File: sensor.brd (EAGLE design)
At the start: 15.8 x 15.8 mm, 16 parts

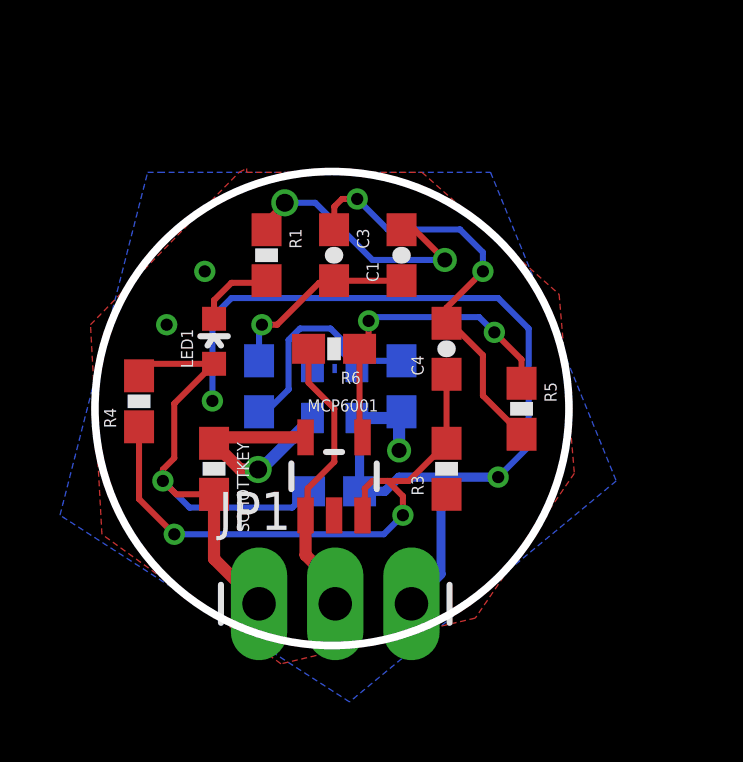
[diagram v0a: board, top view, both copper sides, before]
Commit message: sensor: fix apds-9008 package error
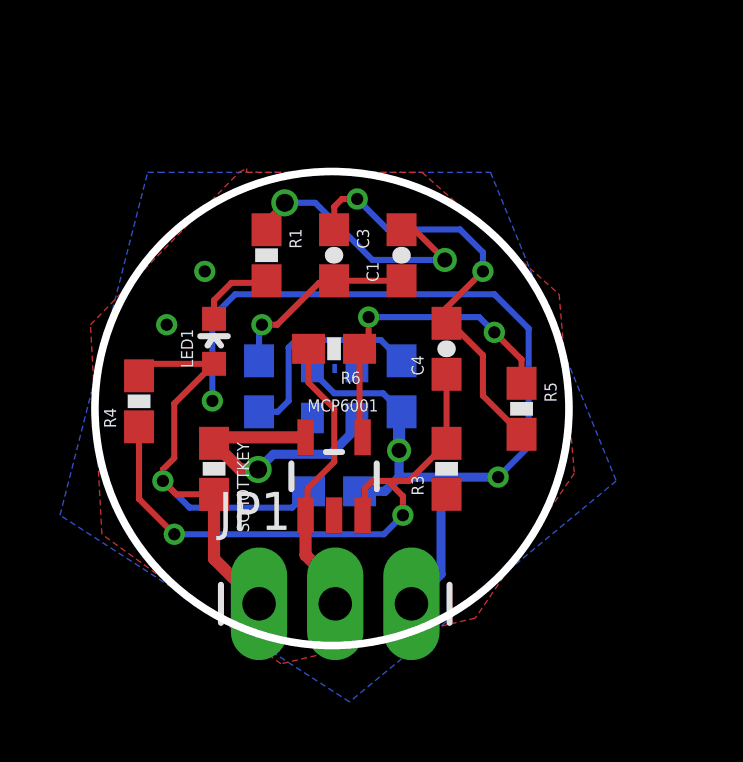
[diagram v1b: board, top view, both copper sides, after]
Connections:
- net GND: now also APDS1.P$4; no longer APDS1.P$3
- net N$7: now also APDS1.P$6; no longer APDS1.P$4
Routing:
- net VDD: track 7.48 -> 9.16 mm
- net GND: track 43.3 -> 44.1 mm
- net N$7: track 7.72 -> 8.52 mm
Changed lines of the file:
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@@
 <wire x1="4.5" y1="7.35" x2="4.7001" y2="7.5501" width="0.4064" layer="1"/>
 <wire x1="4.7001" y1="7.5501" x2="7.55" y2="7.5501" width="0.4064" layer="1"/>
-<wire x1="7.779340625" y1="8.193378125" x2="6.0629625" y2="6.477" width="0.4064" layer="16"/>
-<wire x1="6.0629625" y1="6.477" x2="5.969" y2="6.477" width="0.254" layer="16"/>
 <via x="5.969" y="6.477" extent="1-16" drill="0.6"/>
 <wire x1="5.969" y1="6.477" x2="5.373" y2="6.477" width="0.4064" layer="1"/>
 <wire x1="5.373" y1="6.477" x2="4.5" y2="7.35" width="0.4064" layer="1"/>
+<wire x1="9.260340625" y1="8.193378125" x2="9.260340625" y2="7.863340625" width="0.3048" layer="16"/>
+<wire x1="9.260340625" y1="7.863340625" x2="8.382" y2="6.985" width="0.3048" layer="16"/>
+<wire x1="8.382" y1="6.985" x2="6.477" y2="6.985" width="0.3048" layer="16"/>
+<wire x1="6.477" y1="6.985" x2="5.969" y2="6.477" width="0.3048" layer="16"/>
 </signal>
 <signal name="OUT">
@@
 <contactref element="C2" pad="2"/>
 <contactref element="R2" pad="2"/>
-<contactref element="APDS1" pad="P$4"/>
-<wire x1="6" y1="8.4" x2="6.241" y2="8.4" width="0.2032" layer="16"/>
-<wire x1="6.241" y1="8.4" x2="6.985" y2="9.144" width="0.2032" layer="16"/>
-<wire x1="6.985" y1="9.144" x2="6.985" y2="10.795" width="0.2032" layer="16"/>
-<wire x1="6.985" y1="10.795" x2="7.366" y2="11.176" width="0.2032" layer="16"/>
-<wire x1="7.366" y1="11.176" x2="8.382" y2="11.176" width="0.2032" layer="16"/>
-<wire x1="8.382" y1="11.176" x2="8.763" y2="10.795" width="0.2032" layer="16"/>
-<wire x1="8.763" y1="10.795" x2="8.763" y2="10.39071875" width="0.2032" layer="16"/>
-<wire x1="8.763" y1="10.39071875" x2="9.260340625" y2="9.893378125" width="0.2032" layer="16"/>
-<wire x1="10.75" y1="10.1" x2="9.4669625" y2="10.1" width="0.2032" layer="16"/>
-<wire x1="9.4669625" y1="10.1" x2="9.260340625" y2="9.893378125" width="0.2032" layer="16"/>
+<contactref element="APDS1" pad="P$6"/>
+<wire x1="10.728" y1="10.1" x2="10.75" y2="10.1" width="0.2032" layer="16"/>
+<wire x1="6" y1="8.4" x2="6.622" y2="8.4" width="0.2032" layer="16"/>
+<wire x1="6.622" y1="8.4" x2="6.985" y2="8.763" width="0.2032" layer="16"/>
+<wire x1="6.985" y1="8.763" x2="6.985" y2="10.541" width="0.2032" layer="16"/>
+<wire x1="6.985" y1="10.541" x2="7.239" y2="10.795" width="0.2032" layer="16"/>
+<wire x1="7.239" y1="10.795" x2="9.144" y2="10.795" width="0.2032" layer="16"/>
+<wire x1="9.144" y1="10.795" x2="9.652" y2="10.795" width="0.2032" layer="16"/>
+<wire x1="10.055" y1="10.795" x2="10.75" y2="10.1" width="0.2032" layer="16"/>
+<wire x1="10.055" y1="10.795" x2="9.652" y2="10.795" width="0.2032" layer="16"/>
+<wire x1="9.652" y1="10.795" x2="9.398" y2="10.541" width="0.2032" layer="16"/>
+<wire x1="9.144" y1="10.795" x2="9.398" y2="10.541" width="0.2032" layer="16"/>
+<wire x1="9.398" y1="10.541" x2="9.398" y2="10.0310375" width="0.2032" layer="16"/>
+<wire x1="9.398" y1="10.0310375" x2="9.260340625" y2="9.893378125" width="0.2032" layer="16"/>
 </signal>
 <signal name="N$8">
@@
 <contactref element="MCP6001" pad="4"/>
 <via x="13.843" y="11.049" extent="1-16" drill="0.4064"/>
-<wire x1="9.779" y1="11.557" x2="9.652" y2="11.43" width="0.2032" layer="16"/>
-<via x="9.652" y="11.43" extent="1-16" drill="0.4064"/>
-<wire x1="9.652" y1="11.43" x2="9.652" y2="10.802" width="0.2032" layer="1"/>
+<via x="9.652" y="11.557" extent="1-16" drill="0.4064"/>
+<wire x1="9.652" y1="11.557" x2="9.652" y2="10.802" width="0.2032" layer="1"/>
 <wire x1="9.652" y1="10.802" x2="9.35" y2="10.5" width="0.2032" layer="1"/>
 <wire x1="9.35" y1="10.5" x2="9.35" y2="7.6501" width="0.2032" layer="1"/>
 <wire x1="9.35" y1="7.6501" x2="9.45" y2="7.5501" width="0.2032" layer="1"/>
-<wire x1="9.779" y1="11.557" x2="13.335" y2="11.557" width="0.2032" layer="16"/>
+<wire x1="9.652" y1="11.557" x2="13.335" y2="11.557" width="0.2032" layer="16"/>
 <wire x1="13.335" y1="11.557" x2="13.843" y2="11.049" width="0.2032" layer="16"/>
 <wire x1="13.843" y1="11.049" x2="14.75" y2="10.142" width="0.2032" layer="1"/>
@@
 <contactref element="R3" pad="1"/>
 <contactref element="MCP6001" pad="2"/>
-<contactref element="APDS1" pad="P$3"/>
 <polygon width="0.2032" layer="1" spacing="0.3048" isolate="0.254">
 <vertex x="5.588" y="16.383"/>
@@
 </polygon>
 <via x="4.445" y="8.763" extent="1-16" drill="0.4064"/>
-<wire x1="9.260340625" y1="8.193378125" x2="10.668" y2="8.193378125" width="0.4064" layer="16"/>
 <wire x1="10.75" y1="8.193378125" x2="10.75" y2="8.4" width="0.4064" layer="16"/>
 <wire x1="10.75" y1="8.193378125" x2="10.668" y2="8.193378125" width="0.4064" layer="16"/>
 <wire x1="10.668" y1="8.193378125" x2="10.668" y2="7.112" width="0.4064" layer="16"/>
 <via x="13.97" y="6.223" extent="1-16" drill="0.4064"/>
-<wire x1="9.260340625" y1="8.193378125" x2="9.35" y2="8.193378125" width="0.3048" layer="16"/>
-<wire x1="9.35" y1="8.193378125" x2="9.35" y2="5.75" width="0.3048" layer="16"/>
 <wire x1="9.35" y1="5.75" x2="10.195" y2="5.75" width="0.3048" layer="16"/>
 <wire x1="10.195" y1="5.75" x2="10.668" y2="6.223" width="0.3048" layer="16"/>
@@
 <wire x1="11.185" y1="14.469" x2="10.75" y2="14.469" width="0.2032" layer="1"/>
 <wire x1="4.445" y1="8.763" x2="4.445" y2="11.557" width="0.2032" layer="16"/>
-<wire x1="4.445" y1="11.557" x2="5.08" y2="12.192" width="0.2032" layer="16"/>
-<wire x1="5.08" y1="12.192" x2="13.97" y2="12.192" width="0.2032" layer="16"/>
-<wire x1="13.97" y1="12.192" x2="14.986" y2="11.176" width="0.2032" layer="16"/>
+<wire x1="4.445" y1="11.557" x2="5.207" y2="12.319" width="0.2032" layer="16"/>
+<wire x1="5.207" y1="12.319" x2="13.843" y2="12.319" width="0.2032" layer="16"/>
+<wire x1="13.843" y1="12.319" x2="14.986" y2="11.176" width="0.2032" layer="16"/>
 <wire x1="14.986" y1="11.176" x2="14.986" y2="7.239" width="0.2032" layer="16"/>
 <wire x1="14.986" y1="7.239" x2="13.97" y2="6.223" width="0.2032" layer="16"/>
+<contactref element="APDS1" pad="P$4"/>
+<wire x1="10.668" y1="7.112" x2="10.668" y2="6.223" width="0.3048" layer="16"/>
+<wire x1="10.75" y1="8.493378125" x2="10.75" y2="8.4" width="0.254" layer="16"/>
+<wire x1="7.779340625" y1="9.893378125" x2="7.779340625" y2="9.746659375" width="0.2032" layer="16"/>
+<wire x1="7.779340625" y1="9.746659375" x2="8.509" y2="9.017" width="0.2032" layer="16"/>
+<wire x1="8.509" y1="9.017" x2="10.133" y2="9.017" width="0.2032" layer="16"/>
+<wire x1="10.133" y1="9.017" x2="10.75" y2="8.4" width="0.2032" layer="16"/>
 </signal>
 </signals>

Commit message: sensor: update brd into a 20*20 rectangle
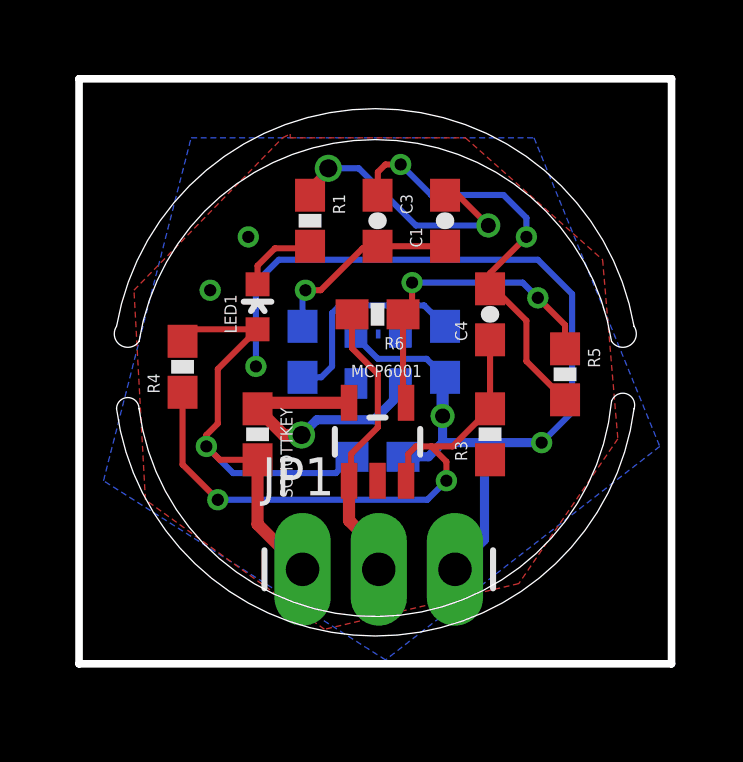
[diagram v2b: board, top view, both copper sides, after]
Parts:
- moved C2 1.85 mm to (7.45, 10.4)
- moved LED1 1.85 mm to (5.95, 11.9)
- moved R1 1.85 mm to (7.70, 14.8)
- moved R4 1.85 mm to (3.45, 9.90)
- moved SCHOTTKEY 1.85 mm to (5.95, 7.65)
- moved JP1 1.85 mm to (7.45, 3.15)
- moved APDS1 1.85 mm to (9.95, 10.2)
- moved C1 1.85 mm to (12.2, 14.8)
- moved C3 1.85 mm to (9.95, 14.8)
- moved C4 1.85 mm to (13.7, 11.7)
- moved C5 1.85 mm to (9.95, 6.90)
- moved MCP6001 1.85 mm to (9.95, 7.40)
- moved R2 1.85 mm to (12.2, 10.4)
- moved R3 1.85 mm to (13.7, 7.65)
- moved R5 1.85 mm to (16.2, 9.65)
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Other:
- board size 15.8 x 15.8 mm -> 19.8 x 19.5 mm
- board text added: "APDS1"
- board text added: "C1"
- board text added: "C2"
- board text added: "C3"
- board text added: "C4"
- board text added: "C5"
- board text added: "JP1"
- board text added: "LED1"
- board text added: "MCP6001"
- board text added: "R1"
- board text added: "R2"
- board text added: "R3"
- board text added: "R4"
- board text added: "R5"
- board text added: "R6"
- board text added: "SCHOTTKEY"

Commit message: sensor: correct schematic and refine layout
1. Replace fake schottkey with a *real* one.
2. Refine polygon.
3. Refine dimension.
4. Refine panel.
5. Add more blowholes (vias).
6. Slightly refine some wires.
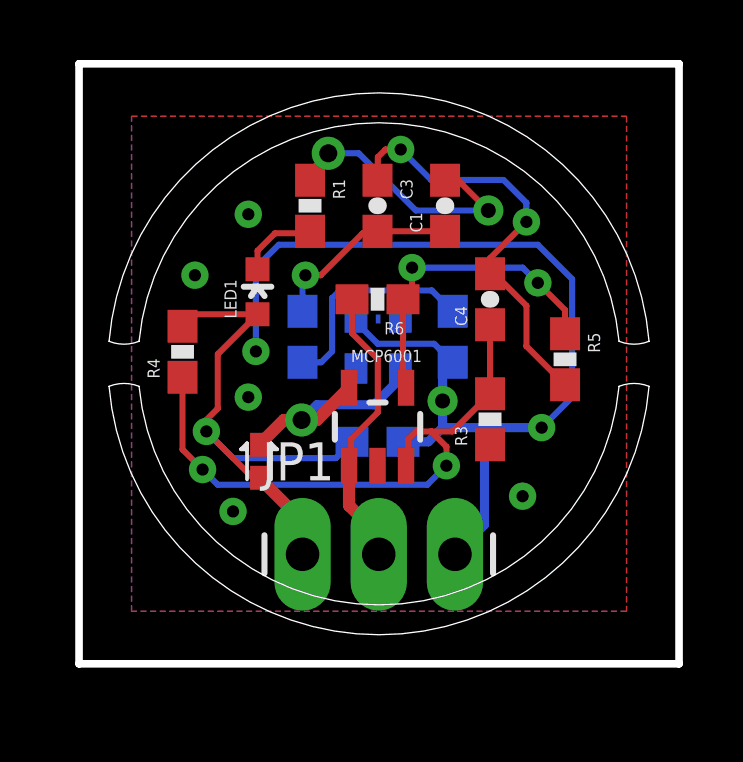
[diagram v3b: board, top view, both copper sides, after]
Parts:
- removed SCHOTTKEY: 0, SparkFun-Resistors:0603-RES
- added D1: RB751, SparkFun-DiscreteSemi:SOD-523
- moved R2 0.56 mm to (12.5, 10.9)
- moved APDS1 0.50 mm to (9.95, 10.7)
- moved C1 0.50 mm to (12.2, 15.3)
- moved C2 0.50 mm to (7.45, 10.9)
- moved C3 0.50 mm to (9.95, 15.3)
- moved C4 0.50 mm to (13.7, 12.2)
- moved C5 0.50 mm to (9.95, 7.40)
- moved JP1 0.50 mm to (7.45, 3.65)
- moved LED1 0.50 mm to (5.95, 12.4)
- moved MCP6001 0.50 mm to (9.95, 7.90)
- moved R1 0.50 mm to (7.70, 15.3)
- moved R3 0.50 mm to (13.7, 8.15)
- moved R4 0.50 mm to (3.45, 10.4)
- moved R5 0.50 mm to (16.2, 10.2)
- moved R6 0.50 mm to (9.95, 12.2)
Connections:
- net VCC: now also D1.A; no longer SCHOTTKEY.2
- net VDD: now also D1.C; no longer SCHOTTKEY.1
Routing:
- net VDD: track 9.16 -> 7.98 mm
- net VCC: track 18.9 -> 18.3 mm
- net GND: track 44.1 -> 44.7 mm, vias 7 -> 10
- net N$7: track 8.52 -> 9.02 mm
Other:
- board size 19.8 x 19.5 mm -> 20 x 20 mm

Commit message: sensor: update lbr and correct design
1. Add a reverse mount led.
2. Update output pad.
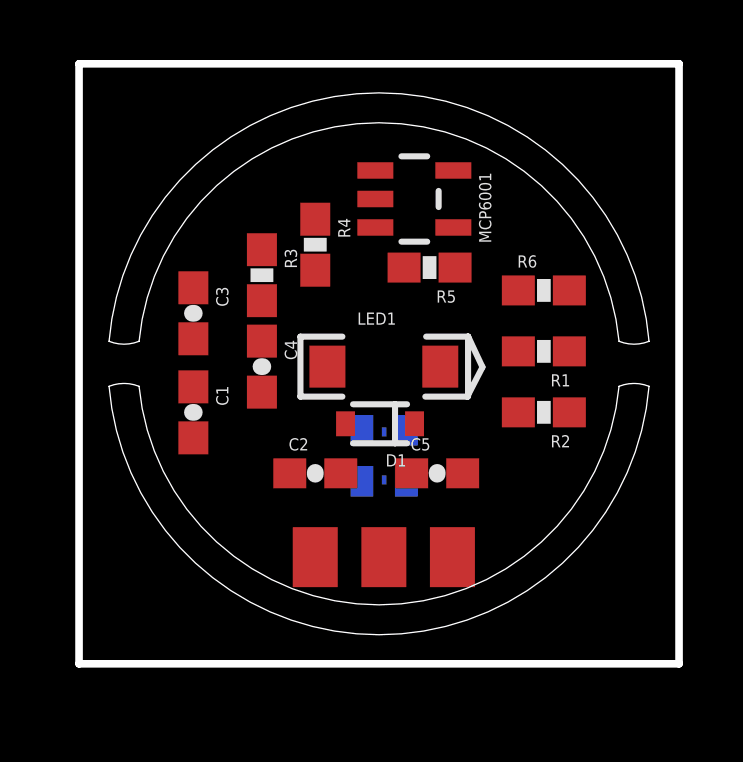
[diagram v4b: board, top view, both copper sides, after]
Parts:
- removed JP1: (no value), SparkFun-Connectors:1X03_LONGPADS
- added GND, OUT, VCC: M01SMD-4.5X1.5, SparkFun-Connectors:PAD-1.5X4.5
- D1: value RB751 -> BAT20JFILM; device SparkFun-DiscreteSemi:SOD-523 -> SparkFun-DiscreteSemi:SOD-323
- LED1: device SparkFun-LED:LED-0603 -> librae:LED-1206-REVERSE-MOUNT
- moved C1 10.9 mm to (3.81, 8.38), turned to 270 degrees
- moved R1 9.18 mm to (15.5, 10.4), turned to 180 degrees
- moved R3 8.99 mm to (6.10, 13.0), turned to 270 degrees
- moved C4 7.93 mm to (6.10, 9.91), turned to 270 degrees
- moved MCP6001 7.69 mm to (11.2, 15.5), turned to 270 degrees
- moved C3 7.11 mm to (3.81, 11.7)
- moved R4 5.68 mm to (7.87, 14.0), turned to 270 degrees
- moved R6 5.55 mm to (15.5, 12.4), turned to 0 degrees
- moved R5 5.45 mm to (11.7, 13.2), turned to 180 degrees
- moved LED1 4.89 mm to (10.2, 9.91)
- moved C2 4.57 mm to (7.87, 6.35), flipped to the top, turned to 0 degrees
- moved D1 4.22 mm to (10.0, 8.00), turned to 180 degrees
- moved R2 3.95 mm to (15.5, 8.38), flipped to the top, turned to 180 degrees
- moved APDS1 3.77 mm to (10.2, 6.89)
- moved C5 2.25 mm to (11.9, 6.35), flipped to the top, turned to 0 degrees
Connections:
- net GND: now also GND.P$1; no longer JP1.3
- net OUT: now also OUT.P$1; no longer JP1.2
- net VCC: now also D1.2, VCC.P$1; no longer D1.A, JP1.1
- net VDD: now also D1.1; no longer D1.C
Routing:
- net GND: track 44.7 -> 0.00 mm, vias 10 -> 0
- net N$10: track 19.9 -> 0.00 mm, vias 2 -> 0
- net VCC: track 18.3 -> 0.00 mm, vias 1 -> 0
- net N$9: track 14.3 -> 0.00 mm, vias 2 -> 0
- net N$6: track 10.6 -> 0.00 mm, vias 2 -> 0
- net OUT: track 9.66 -> 0.00 mm
- net N$7: track 9.02 -> 0.00 mm
- net VDD: track 7.98 -> 0.00 mm, vias 1 -> 0
- net N$8: track 6.50 -> 0.00 mm, vias 1 -> 0
- net N$3: track 3.03 -> 0.00 mm
- removed copper zone on layer 1, net GND
- removed copper zone on layer 16, net GND

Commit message: sensor: update pcb layout
Mainly correct LED position and work mechanism.
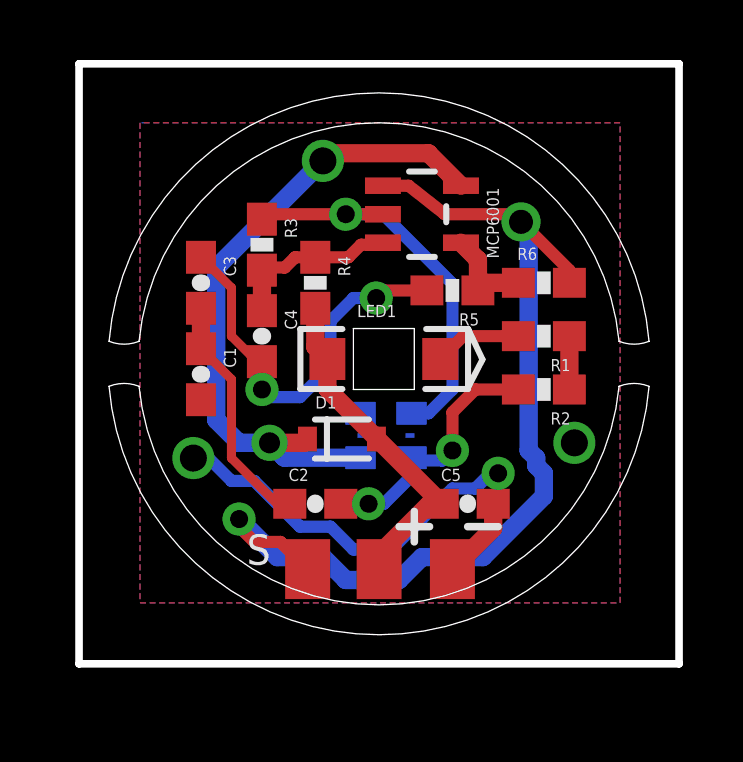
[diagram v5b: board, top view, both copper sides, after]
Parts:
- moved OUT 4.84 mm to (7.62, 3.16)
- moved GND 4.59 mm to (12.4, 3.16)
- moved C5 1.44 mm to (13.0, 5.33)
- moved D1 1.37 mm to (8.76, 7.49), turned to 0 degrees
- moved C1 1.30 mm to (4.06, 9.65)
- moved R4 1.27 mm to (7.87, 12.7)
- moved R5 1.08 mm to (12.4, 12.4)
- moved C3 1.05 mm to (4.06, 12.7)
- moved C2 1.02 mm to (7.87, 5.33)
- moved C4 1.02 mm to (6.10, 10.9)
- moved R3 1.02 mm to (6.10, 14.0)
- moved R2 0.76 mm to (15.5, 9.14)
- moved APDS1 0.74 mm to (10.2, 7.63), turned to 270 degrees
- moved MCP6001 0.57 mm to (11.4, 15.0)
- moved R1 0.51 mm to (15.5, 10.9)
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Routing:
- net OUT: track 0.00 -> 32.5 mm, vias 0 -> 2
- net GND: track 0.00 -> 32.2 mm, vias 0 -> 4
- net VDD: track 0.00 -> 21.9 mm, vias 0 -> 2
- net N$9: track 0.00 -> 13.3 mm, vias 0 -> 2
- net VCC: track 0.00 -> 11.6 mm
- net N$7: track 0.00 -> 8.62 mm, vias 0 -> 2
- net N$8: track 0.00 -> 7.99 mm
- net N$10: track 0.00 -> 5.76 mm
- net N$6: track 0.00 -> 3.28 mm
- net N$3: track 0.00 -> 2.92 mm
- added copper zone on layer 1, net GND
- added copper zone on layer 16, net GND
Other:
- outline, holes or cut-outs redrawn
- board text added: "S"

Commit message: sensor: increase led hole size
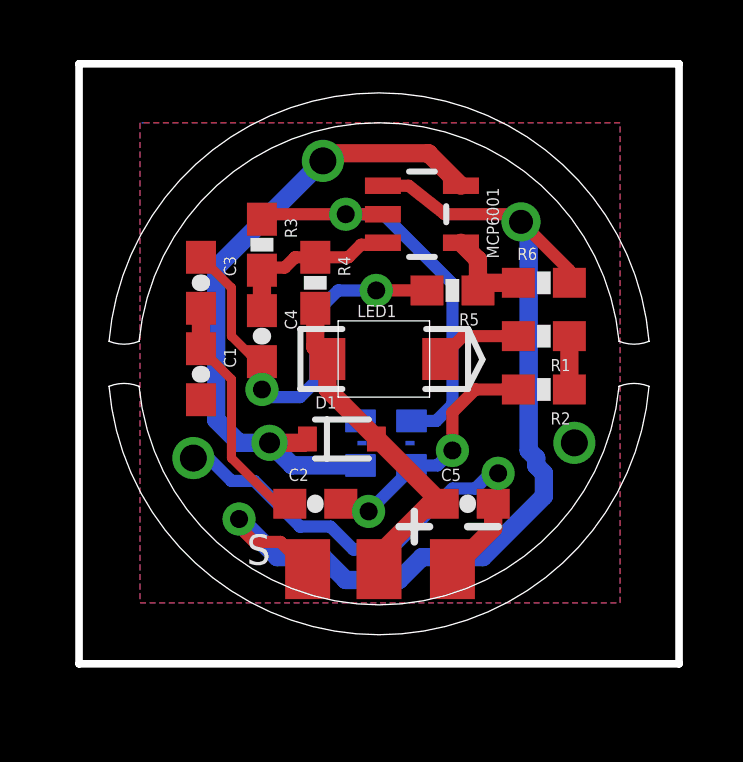
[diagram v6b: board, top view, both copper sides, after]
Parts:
- moved APDS1 0.25 mm to (10.2, 7.38)
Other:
- outline, holes or cut-outs redrawn
